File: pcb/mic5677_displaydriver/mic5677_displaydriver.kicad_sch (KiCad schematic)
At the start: 45 parts, among them J1 Segment DIP7, J2 H, J3 Sec, J4 Common Cathode Enable, Q1 D45H8G, Q10 BC546, Q11 BC546, Q12 BC546, Q13 BC546, Q14 BC546, Q15 BC546, Q16 BC546, Q17 BC546, Q18 BC546, Q2 D45H8G, Q3 D45H8G, Q4 D45H8G, Q5 D45H8G, Q6 D45H8G, Q7 D45H8G, Q8 D45H8G, Q9 D45H8G, U1 74HC595, U2 74HC595, U3 74HC02

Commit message: Added some component documentation
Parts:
- added U4: LM7805_TO220, Package_SO:SOIC-8_3.9x4.9mm_P1.27mm, symbol Regulator_Linear:LM7805_TO220
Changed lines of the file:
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@@
+    )
+  )
+  (symbol (lib_id "Regulator_Linear:LM7805_TO220") (at 104.14 160.02 0) (unit 1)
+    (in_bom yes) (on_board yes) (dnp no) (fields_autoplaced)
+    (property "Reference" "U4" (at 104.14 153.67 0)
+      (effects (font (size 1.27 1.27)))
+    )
+    (property "Value" "LM7805_TO220" (at 104.14 156.21 0)
+      (effects (font (size 1.27 1.27)))
+    )
+    (property "Footprint" "Package_SO:SOIC-8_3.9x4.9mm_P1.27mm" (at 104.14 154.305 0)
+      (effects (font (size 1.27 1.27) italic) hide)
+    )
+    (property "Datasheet" "https://www.onsemi.cn/PowerSolutions/document/MC7800-D.PDF" (at 104.14 161.29 0)
+      (effects (font (size 1.27 1.27)) hide)
+    )
+    (pin "1")
+    (pin "2")
+    (pin "3")
+    (instances
+      (project "mic5677_displaydriver"
+        (path "/904d3710-a02f-4e23-8828-29b05a2e6582"
+          (reference "U4") (unit 1)
+        )
+      )
     )
   )

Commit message: Updated display pcb
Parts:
- removed J1: Segment DIP7, symbol Connector:Conn_01x07_Socket
- removed U4: LM7805_TO220, Package_SO:SOIC-8_3.9x4.9mm_P1.27mm, symbol Regulator_Linear:LM7805_TO220
- added C1: 10u, Capacitor_THT:C_Disc_D3.8mm_W2.6mm_P2.50mm, symbol Device:C
- added C2: 22u, Capacitor_THT:C_Disc_D3.8mm_W2.6mm_P2.50mm, symbol Device:C
- added C3, C4, C5: 100n, Capacitor_THT:C_Disc_D3.8mm_W2.6mm_P2.50mm, symbol Device:C
- added D1: PWR, LED_THT:LED_D3.0mm, symbol Device:LED
- added H1, H2, H3, H4: MountingHole, MountingHole:MountingHole_5.3mm_M5, symbol Mechanical:MountingHole
- added J1, J2: Segment DIP14, Package_DIP:DIP-14_W7.62mm_Socket, symbol Connector:Conn_01x14_Socket
- added J6: PSU Socket, Connector_PinHeader_2.54mm:PinHeader_1x03_P2.54mm_Vertical, symbol Connector:Conn_01x03_Socket
- added J7: 8P8C, Connector_RJ:RJ45_Amphenol_54602-x08_Horizontal, symbol Connector:8P8C
- added Q19, Q20, Q21, Q22, Q23: BC546, Package_TO_SOT_THT:TO-92_Inline, symbol Transistor_BJT:BC546
- added R1: 3k3, Resistor_THT:R_Axial_DIN0204_L3.6mm_D1.6mm_P7.62mm_Horizontal, symbol Device:R
- added R20, R22, R24, R26, R28, R30, R31, R32, R33, R34: 470k, Resistor_THT:R_Axial_DIN0204_L3.6mm_D1.6mm_P7.62mm_Horizontal, symbol Device:R
- added R21, R23, R25, R27, R29: 22k, Resistor_THT:R_Axial_DIN0204_L3.6mm_D1.6mm_P7.62mm_Horizontal, symbol Device:R
- added U1: L7805, Package_TO_SOT_THT:TO-220-3_Vertical, symbol Regulator_Linear:L7805
- D2: renamed from D1; footprint (none) -> LED_THT:LED_D3.0mm
- J3: renamed from J2; footprint (none) -> Connector_PinHeader_2.54mm:PinHeader_1x01_P2.54mm_Vertical
- J4: renamed from J3; footprint (none) -> Connector_PinHeader_2.54mm:PinHeader_1x01_P2.54mm_Vertical
- J5: renamed from J4; footprint (none) -> Connector_PinHeader_2.54mm:PinHeader_1x08_P2.54mm_Vertical
- Q1, Q2, Q3, Q4, Q5, Q6, Q7, Q8, Q9: footprint On_Semiconductor-D45H8G-* -> eec:On_Semiconductor-D45H8G-Manufacturer_Recommended
- R10: renamed from R9; footprint (none) -> Resistor_THT:R_Axial_DIN0204_L3.6mm_D1.6mm_P7.62mm_Horizontal
- R11: renamed from R10; footprint (none) -> Resistor_THT:R_Axial_DIN0204_L3.6mm_D1.6mm_P7.62mm_Horizontal
- R12: renamed from R11; footprint (none) -> Resistor_THT:R_Axial_DIN0204_L3.6mm_D1.6mm_P7.62mm_Horizontal
- R13: renamed from R12; footprint (none) -> Resistor_THT:R_Axial_DIN0204_L3.6mm_D1.6mm_P7.62mm_Horizontal
- R14: renamed from R13; footprint (none) -> Resistor_THT:R_Axial_DIN0204_L3.6mm_D1.6mm_P7.62mm_Horizontal
- R15: renamed from R14; footprint (none) -> Resistor_THT:R_Axial_DIN0204_L3.6mm_D1.6mm_P7.62mm_Horizontal
- R16: renamed from R15; footprint (none) -> Resistor_THT:R_Axial_DIN0204_L3.6mm_D1.6mm_P7.62mm_Horizontal
- R17: renamed from R16; footprint (none) -> Resistor_THT:R_Axial_DIN0204_L3.6mm_D1.6mm_P7.62mm_Horizontal
- R18: renamed from R17; footprint (none) -> Resistor_THT:R_Axial_DIN0204_L3.6mm_D1.6mm_P7.62mm_Horizontal
- R19: renamed from R18; footprint (none) -> Resistor_THT:R_Axial_DIN0204_L3.6mm_D1.6mm_P7.62mm_Horizontal
- R2: renamed from R1; footprint (none) -> Resistor_THT:R_Axial_DIN0204_L3.6mm_D1.6mm_P7.62mm_Horizontal
- R3: renamed from R2; footprint (none) -> Resistor_THT:R_Axial_DIN0204_L3.6mm_D1.6mm_P7.62mm_Horizontal
- R35: renamed from R19; footprint (none) -> Resistor_THT:R_Axial_DIN0204_L3.6mm_D1.6mm_P7.62mm_Horizontal
- R4: renamed from R3; footprint (none) -> Resistor_THT:R_Axial_DIN0204_L3.6mm_D1.6mm_P7.62mm_Horizontal
- R5: renamed from R4; footprint (none) -> Resistor_THT:R_Axial_DIN0204_L3.6mm_D1.6mm_P7.62mm_Horizontal
- R6: renamed from R5; footprint (none) -> Resistor_THT:R_Axial_DIN0204_L3.6mm_D1.6mm_P7.62mm_Horizontal
- R7: renamed from R6; footprint (none) -> Resistor_THT:R_Axial_DIN0204_L3.6mm_D1.6mm_P7.62mm_Horizontal
- R8: renamed from R7; footprint (none) -> Resistor_THT:R_Axial_DIN0204_L3.6mm_D1.6mm_P7.62mm_Horizontal
- R9: renamed from R8; footprint (none) -> Resistor_THT:R_Axial_DIN0204_L3.6mm_D1.6mm_P7.62mm_Horizontal
- U4: renamed from U3; footprint (none) -> Package_DIP:DIP-14_W7.62mm_Socket
- renumbered U1 to U3
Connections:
- net +5V: now also C2.1, C3.1, C4.1, C5.1, D1.2 (A), R21.1, R23.1, R25.1, R27.1, R29.1, U1.3 (OUT)
- net GND: now also C1.2, C2.2, C3.2, C4.2, C5.2, J6.2 (Pin_2), J7.7, Q19.3 (E), Q20.3 (E), Q21.3 (E), Q22.3 (E), Q23.3 (E), R1.2, U1.2 (GND)
- net OE: now also Q20.1 (C), R23.2
- net RCLK: now also Q23.1 (C), R29.2
- net SER0: now also Q22.1 (C), R27.2
- net SER1: now also Q19.1 (C), R21.2
- net SRCLK: now also Q21.1 (C), R25.2
- net VDC: now also C1.1, J6.3 (Pin_3), J7.8, R20.1, R22.1, R24.1, R26.1, R28.1, U1.1 (IN)
- net at Q6.3 (E): now also J1.6 (Pin_6), J1.9 (Pin_9), J2.6 (Pin_6), J2.9 (Pin_9)
- net at Q5.3 (E): now also J1.10 (Pin_10), J1.5 (Pin_5), J2.10 (Pin_10), J2.5 (Pin_5)
- net at Q1.3 (E): now also J1.1 (Pin_1), J1.14 (Pin_14), J2.1 (Pin_1), J2.14 (Pin_14)
- net at Q2.3 (E): now also J1.13 (Pin_13), J1.2 (Pin_2), J2.13 (Pin_13), J2.2 (Pin_2)
- net at Q3.3 (E): now also J1.12 (Pin_12), J1.3 (Pin_3), J2.12 (Pin_12), J2.3 (Pin_3)
- net at Q4.3 (E): now also J1.11 (Pin_11), J1.4 (Pin_4), J2.11 (Pin_11), J2.4 (Pin_4)
- net at Q7.3 (E): now also J1.7 (Pin_7), J1.8 (Pin_8), J2.7 (Pin_7), J2.8 (Pin_8)
- new net: Q20.2 (B), R31.2
- new net: D1.1 (K), R1.1
- new net: Q22.2 (B), R33.2
- new net: Q23.2 (B), R34.2
- new net: Q21.2 (B), R32.2
- new net: Q19.2 (B), R30.2
- new net OE_IN: J7.4, R22.2, R31.1
- new net PWR_EN: J6.1 (Pin_1), J7.5
- new net RCLK_IN: J7.1, R28.2, R34.1
- new net SER0_IN: J7.2, R26.2, R33.1
- new net SER1_IN: J7.6, R20.2, R30.1
- new net SRCLK_IN: J7.3, R24.2, R32.1
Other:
- note added: "DIP14 style connectors for ribbon cables"
- note added: "Mounting Holes"
- note added: "Power Supply - Vdc around 28V"
- note added: "Power and Signal inputs"
- note removed: "DIP7 style connector for ribbon cable"
- moved on the sheet: D2, J3, J4, J5, Q1, Q10, Q11, Q12, Q13, Q14, Q15, Q16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

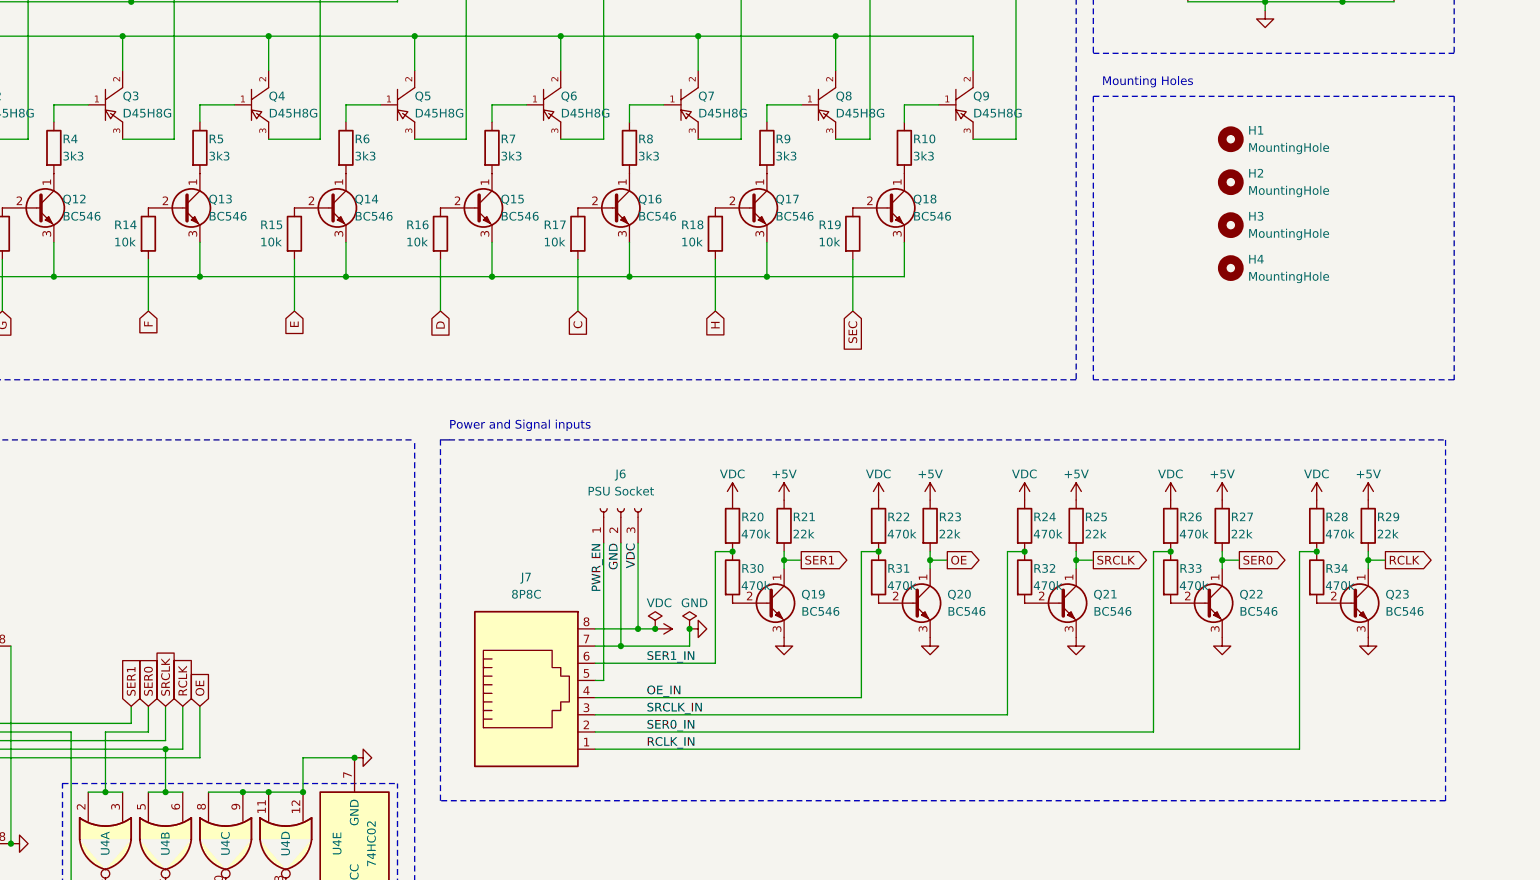
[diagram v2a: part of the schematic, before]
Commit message: Improved display driver pcb
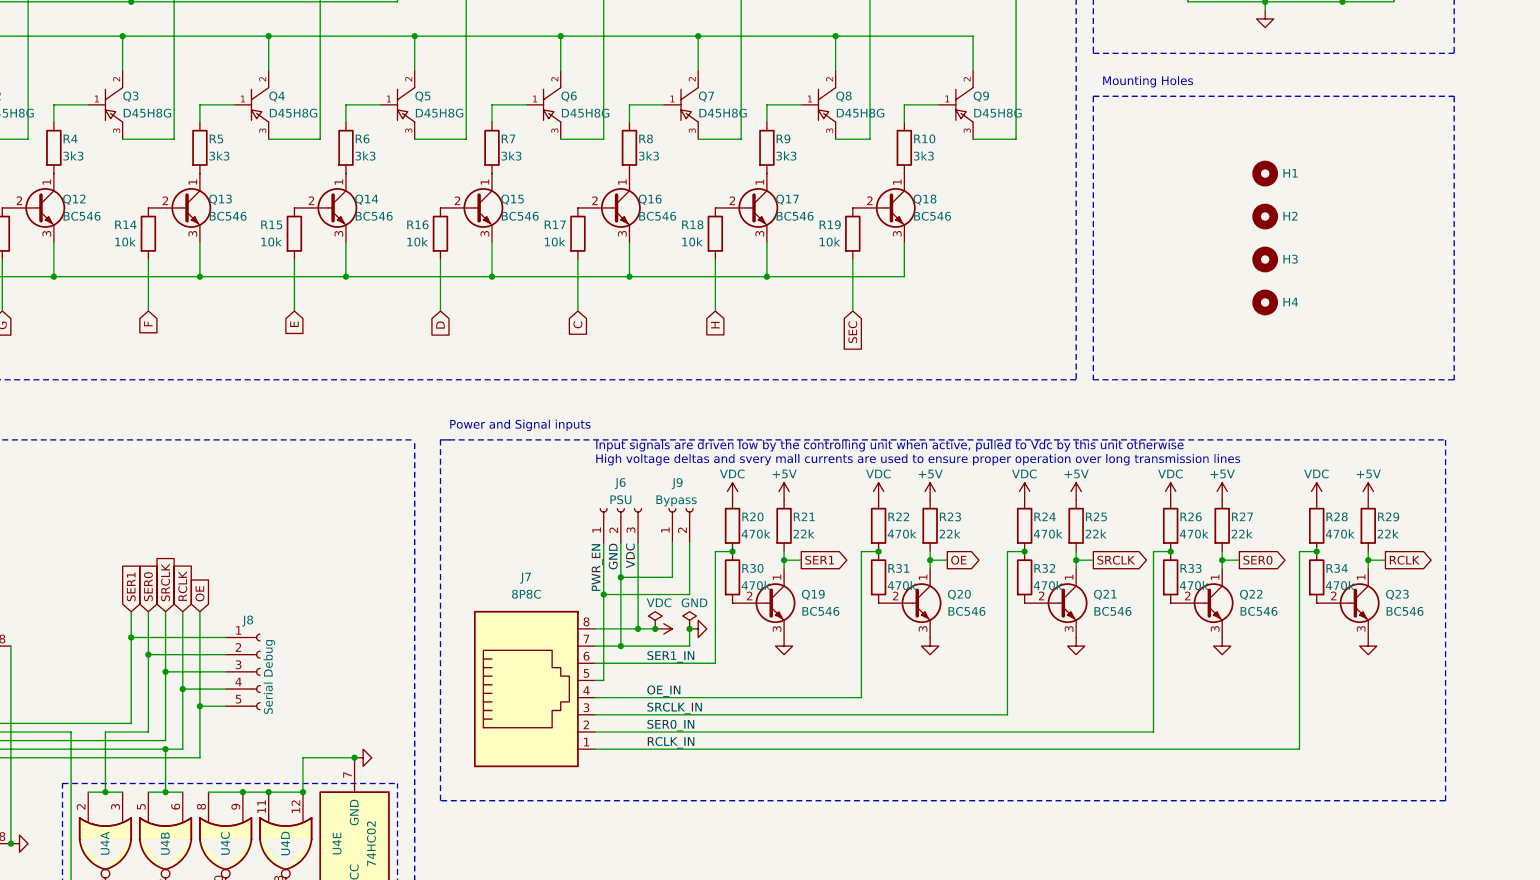
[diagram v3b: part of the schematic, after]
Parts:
- added J8: Serial Debug, Connector_PinHeader_2.54mm:PinHeader_1x05_P2.54mm_Vertical, symbol Connector:Conn_01x05_Socket
- added J9: Bypass, Connector_PinHeader_2.54mm:PinHeader_1x02_P2.54mm_Vertical, symbol Connector:Conn_01x02_Socket
- J6: value PSU Socket -> PSU
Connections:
- net GND: now also J9.1 (Pin_1)
- net OE: now also J8.5 (Pin_5)
- net PWR_EN: now also J9.2 (Pin_2)
- net RCLK: now also J8.4 (Pin_4)
- net SER0: now also J8.2 (Pin_2)
- net SER1: now also J8.1 (Pin_1)
- net SRCLK: now also J8.3 (Pin_3)
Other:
- note added: "Input signals are driven low by the controlling unit when active, pulled to Vdc by this unit otherwise High voltage deltas and svery mall currents are used to ensure proper operation over long transmission lines"
- moved on the sheet: H1, H2, H3, H4

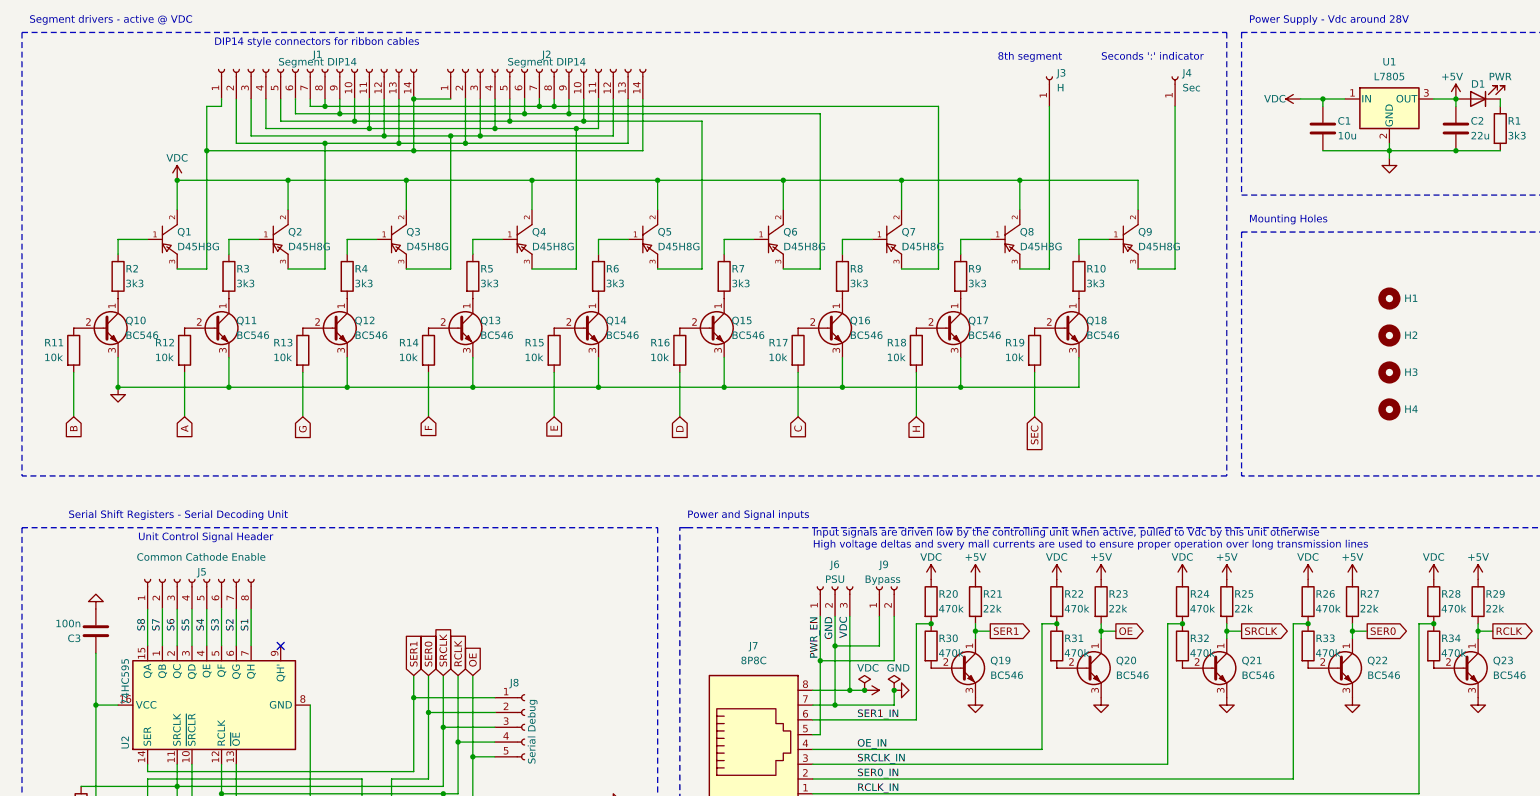
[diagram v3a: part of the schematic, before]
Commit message: Finished display driver pcb
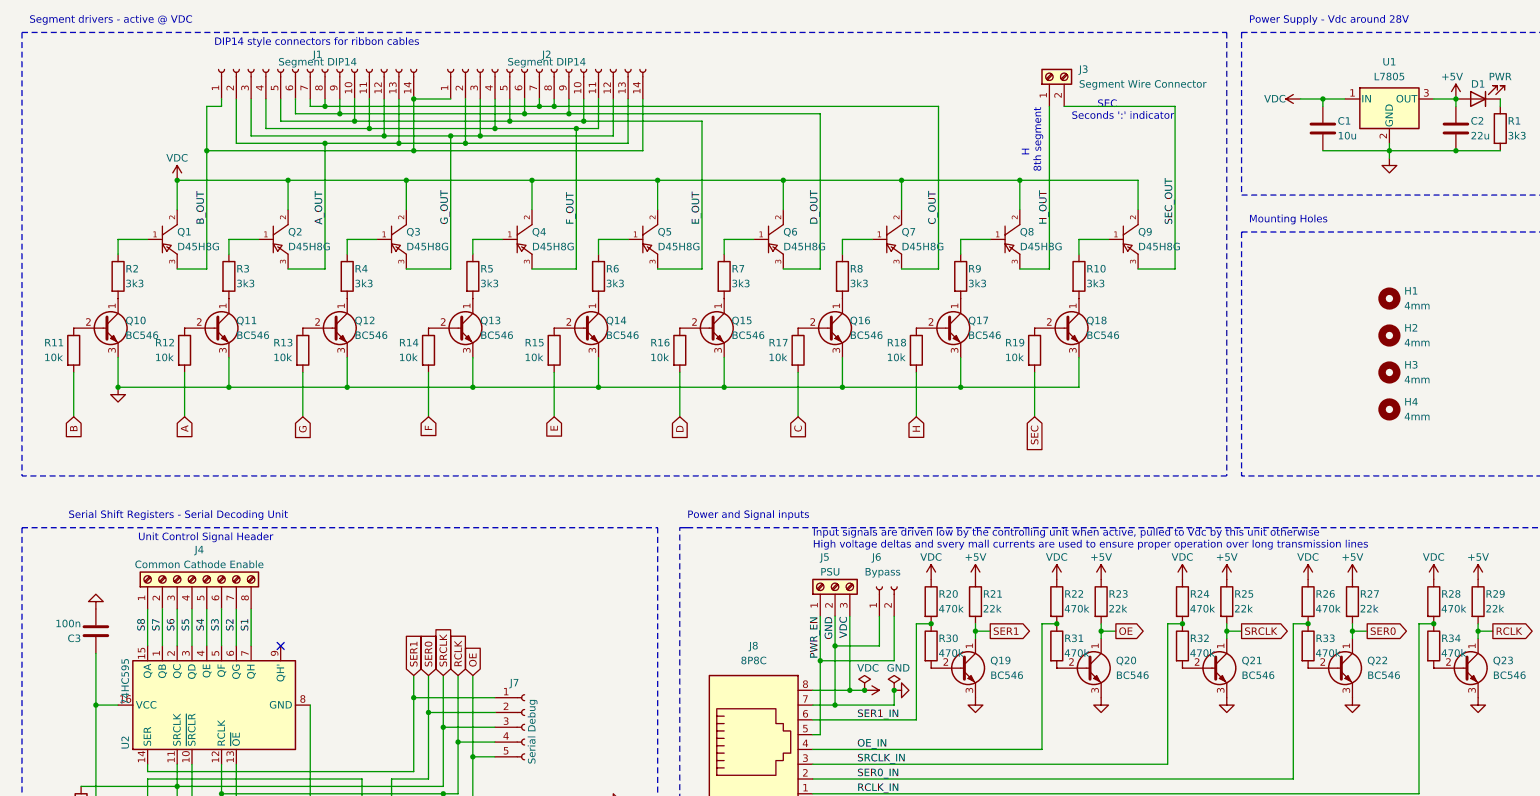
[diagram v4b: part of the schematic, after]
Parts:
- removed J3: H, Connector_PinHeader_2.54mm:PinHeader_1x01_P2.54mm_Vertical, symbol Connector:Conn_01x01_Socket
- removed J4: Sec, Connector_PinHeader_2.54mm:PinHeader_1x01_P2.54mm_Vertical, symbol Connector:Conn_01x01_Socket
- removed J5: Common Cathode Enable, Connector_PinHeader_2.54mm:PinHeader_1x08_P2.54mm_Vertical, symbol Connector:Conn_01x08_Socket
- removed J6: PSU, Connector_PinHeader_2.54mm:PinHeader_1x03_P2.54mm_Vertical, symbol Connector:Conn_01x03_Socket
- added J3: Segment Wire Connector, TerminalBlock:TerminalBlock_bornier-2_P5.08mm, symbol Connector:Screw_Terminal_01x02
- added J4: Common Cathode Enable, TerminalBlock_RND:TerminalBlock_RND_205-00238_1x08_P5.08mm_Horizontal, symbol Connector:Screw_Terminal_01x08
- added J5: PSU, TerminalBlock:TerminalBlock_bornier-3_P5.08mm, symbol Connector:Screw_Terminal_01x03
- H1, H2, H3, H4: value MountingHole -> 4mm; footprint MountingHole:MountingHole_5.3mm_M5 -> MountingHole:MountingHole_4mm
- renumbered J9 to J6, J8 to J7, J7 to J8
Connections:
- net GND: now also J5.2 (Pin_2)
- net PWR_EN: now also J5.1 (Pin_1)
- net S1: now also J4.8 (Pin_8)
- net S2: now also J4.7 (Pin_7)
- net S3: now also J4.6 (Pin_6)
- net S4: now also J4.5 (Pin_5)
- net S5: now also J4.4 (Pin_4)
- net S6: now also J4.3 (Pin_3)
- net S7: now also J4.2 (Pin_2)
- net S8: now also J4.1 (Pin_1)
- net VDC: now also J5.3 (Pin_3)
- net H_OUT: now reaches Q8.3 (E)
- net H_OUT: now also J3.1 (Pin_1)
- net SEC_OUT: now reaches Q9.3 (E)
- net SEC_OUT: now also J3.2 (Pin_2)
- net D_OUT: now reaches J1.6 (Pin_6), J1.9 (Pin_9), J2.6 (Pin_6), J2.9 (Pin_9), Q6.3 (E)
- net E_OUT: now reaches J1.10 (Pin_10), J1.5 (Pin_5), J2.10 (Pin_10), J2.5 (Pin_5), Q5.3 (E)
- net F_OUT: now reaches J1.11 (Pin_11), J1.4 (Pin_4), J2.11 (Pin_11), J2.4 (Pin_4), Q4.3 (E)
- net B_OUT: now reaches J1.1 (Pin_1), J1.14 (Pin_14), J2.1 (Pin_1), J2.14 (Pin_14), Q1.3 (E)
- net G_OUT: now reaches J1.12 (Pin_12), J1.3 (Pin_3), J2.12 (Pin_12), J2.3 (Pin_3), Q3.3 (E)
- net A_OUT: now reaches J1.13 (Pin_13), J1.2 (Pin_2), J2.13 (Pin_13), J2.2 (Pin_2), Q2.3 (E)
- net C_OUT: now reaches J1.7 (Pin_7), J1.8 (Pin_8), J2.7 (Pin_7), J2.8 (Pin_8), Q7.3 (E)
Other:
- note added: "H 8th segment"
- note added: "SEC Seconds ':' indicator"
- note removed: "8th segment"
- note removed: "Seconds ':' indicator"
